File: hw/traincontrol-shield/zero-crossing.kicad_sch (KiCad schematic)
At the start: 3 parts, among them U2 H11AA1

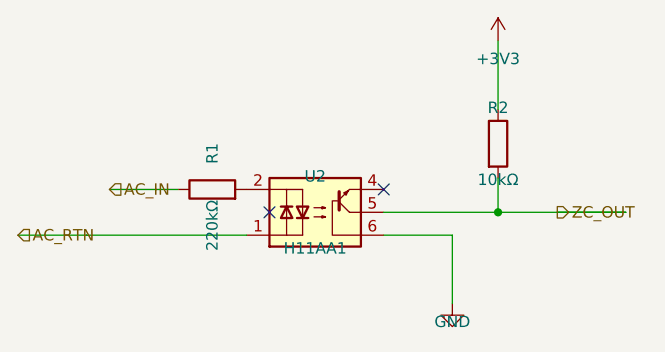
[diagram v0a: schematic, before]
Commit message: Revert "Fix U2 (H11AA1) schematic orientation for conventional NPN layout"
This reverts commit 6bef0f34c2064906dba6c87f8e1f2308b0ec682e.
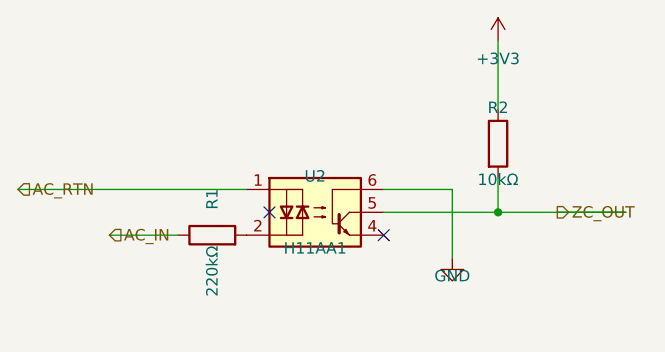
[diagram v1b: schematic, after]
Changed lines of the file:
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@@
 		(lib_id "Isolator:H11AA1")
 		(at 96.52 90.17 0)
-		(mirror x)
 		(unit 1)
 		(exclude_from_sim no)
@@
 	(symbol
 		(lib_id "Device:R")
-		(at 85.09 87.63 90)
+		(at 85.09 92.71 90)
 		(unit 1)
 		(exclude_from_sim no)
@@
 		(dnp no)
 		(property "Reference" "R1"
-			(at 85.09 83.63 0)
+			(at 85.09 88.71 0)
 			(effects (font (size 1.27 1.27)))
 		)
 		(property "Value" "220kΩ"
-			(at 85.09 91.63 0)
+			(at 85.09 96.71 0)
 			(effects (font (size 1.27 1.27)))
 		)
 		(property "Footprint" "Resistor_SMD:R_0603_1608Metric"
-			(at 85.09 87.63 0)
+			(at 85.09 92.71 0)
 			(effects (font (size 1.27 1.27)) (hide yes))
 		)
 		(property "Datasheet" "~"
-			(at 85.09 87.63 0)
+			(at 85.09 92.71 0)
 			(effects (font (size 1.27 1.27)) (hide yes))
 		)
@@
 	)
 	(wire
-		(pts (xy 104.14 92.71000000000001) (xy 111.76 92.71000000000001))
-		(stroke (width 0) (type solid))
-	)
-	(wire
-		(pts (xy 111.76 92.71000000000001) (xy 111.76 100.33000000000001))
+		(pts (xy 104.14 87.63) (xy 111.76 87.63))
+		(stroke (width 0) (type solid))
+	)
+	(wire
+		(pts (xy 111.76 87.63) (xy 111.76 95.25))
 		(stroke (width 0) (type solid))
 	)
 	(symbol
 		(lib_id "power:GND")
-		(at 111.76 100.33000000000001 0)
+		(at 111.76 95.25 0)
 		(unit 1)
 		(exclude_from_sim no)
@@
 		(dnp no)
 		(property "Reference" "#PWR0301"
-			(at 111.76 98.33000000000001 0)
+			(at 111.76 93.25 0)
 			(effects (font (size 1.27 1.27)) (hide yes))
 		)
 		(property "Value" "GND"
-			(at 111.76 102.33000000000001 0)
+			(at 111.76 97.25 0)
 			(effects (font (size 1.27 1.27)))
 		)
 		(property "Footprint" ""
-			(at 111.76 100.33000000000001 0)
+			(at 111.76 95.25 0)
 			(effects (font (size 1.27 1.27)) (hide yes))
 		)
 		(property "Datasheet" ""
-			(at 111.76 100.33000000000001 0)
+			(at 111.76 95.25 0)
 			(effects (font (size 1.27 1.27)) (hide yes))
 		)
@@
 	)
 	(wire
-		(pts (xy 88.89999999999999 92.71000000000001) (xy 71.12 92.71000000000001))
-		(stroke (width 0) (type solid))
-	)
-	(wire
-		(pts (xy 73.66 87.63) (xy 81.28 87.63))
+		(pts (xy 88.89999999999999 87.63) (xy 71.12 87.63))
+		(stroke (width 0) (type solid))
+	)
+	(wire
+		(pts (xy 73.66 92.71) (xy 81.28 92.71))
 		(stroke (width 0) (type solid))
 	)
 	(hierarchical_label "AC_IN"
 		(shape input)
-		(at 73.66 87.63 0)
+		(at 73.66 92.71 0)
 		(fields_autoplaced yes)
 		(effects (font (size 1.27 1.27)) (justify left bottom))
 		(property "Intersheetrefs" "${INTERSHEET_REFS}"
-			(at 73.66 87.63 0)
-			(effects (font (size 1.27 1.27)) (hide yes))
-		)
-	)
-	(wire
-		(pts (xy 63.50000000000001 92.71) (xy 71.12 92.71))
+			(at 73.66 92.71 0)
+			(effects (font (size 1.27 1.27)) (hide yes))
+		)
+	)
+	(wire
+		(pts (xy 63.50000000000001 87.63) (xy 71.12 87.63))
 		(stroke (width 0) (type solid))
 	)
 	(hierarchical_label "AC_RTN"
 		(shape input)
-		(at 63.50000000000001 92.71 0)
+		(at 63.50000000000001 87.63 0)
 		(fields_autoplaced yes)
 		(effects (font (size 1.27 1.27)) (justify left bottom))
 		(property "Intersheetrefs" "${INTERSHEET_REFS}"
-			(at 63.50000000000001 92.71 0)
+			(at 63.50000000000001 87.63 0)
 			(effects (font (size 1.27 1.27)) (hide yes))
 		)
@@
 	)
 	(no_connect
-		(at 104.14 87.63)
+		(at 104.14 92.71000000000001)
 	)
 	(sheet_instances
